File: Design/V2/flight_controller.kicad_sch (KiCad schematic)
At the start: 45 parts, among them J1 Conn_03x08_Odd_Even, J2 Conn_03x08_Odd_Even, U1 STM32H747BIT6

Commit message: power board
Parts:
- removed J1, J2: Conn_03x08_Odd_Even, symbol 3x8_Pin_Header:Conn_03x08_Odd_Even
- removed R10, R9: 4.7K, Resistor_SMD:R_0603_1608Metric_Pad0.98x0.95mm_HandSolder, symbol Device:R
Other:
- note removed: "I2C Pull-Up Resistors"

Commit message: editing bom
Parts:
- BARO1: LCSC Part # (none) -> C5124834
- C42, C43, C44, C47, C48, C49: LCSC Part # (none) -> C14663
- C45: LCSC Part # (none) -> C15849; Manufacturer_Part_Number CL10B105KO8NNNC -> CL10A105KB8NNNC
- C46: LCSC Part # (none) -> C15850; Manufacturer_Name KEMET -> Samsung Electro-Mechanics; Manufacturer_Part_Number C0805C106K8RACTU -> CL21A106KAYNNNE
- FLASH1: Height 0.8 -> (none); Mouser Part Number 454-W25N01GWZEIG -> (none); Mouser Price/Stock https://www.mouser.co.uk/ProductDetail/Winbond/W25N01GWZEIG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 -> (none)
- IMU1: LCSC Part # (none) -> C5368700
- LED3, LED7: value R -> Red; LCSC Part # (none) -> C2286; Manufacturer_Name Lite-On Inc. -> Hubei KENTO Elec; Manufacturer_Part_Number LTST-C191KRKT -> KT-0603R
- LED4: value Y -> Red; LCSC Part # (none) -> C2286; Manufacturer_Name Lite-On Inc. -> Hubei KENTO Elec; Manufacturer_Part_Number LTST-C191KSKT -> KT-0603R
- LED5, LED6: value B -> Red; LCSC Part # (none) -> C2286; Manufacturer_Name Lite-On Inc. -> Hubei KENTO Elec; Manufacturer_Part_Number LTST-C193TBKT-5A -> KT-0603R
- MAG1: LCSC Part # (none) -> C404329
- R13, R14: LCSC Part # (none) -> C25804; Manufacturer_Name TE Connectivity Passive Product -> UNI-ROYAL(Uniroyal Elec); Manufacturer_Part_Number CRGP0603F10K -> 0603WAF1002T5E
- R15, R16, R17, R18, R19: value 330 -> 39; LCSC Part # (none) -> C2907032; Manufacturer_Name TE Connectivity Passive Product -> FOJAN; Manufacturer_Part_Number CRGP0603F330R -> FRC0603F39R0TS
- U1: LCSC Part # (none) -> C730197

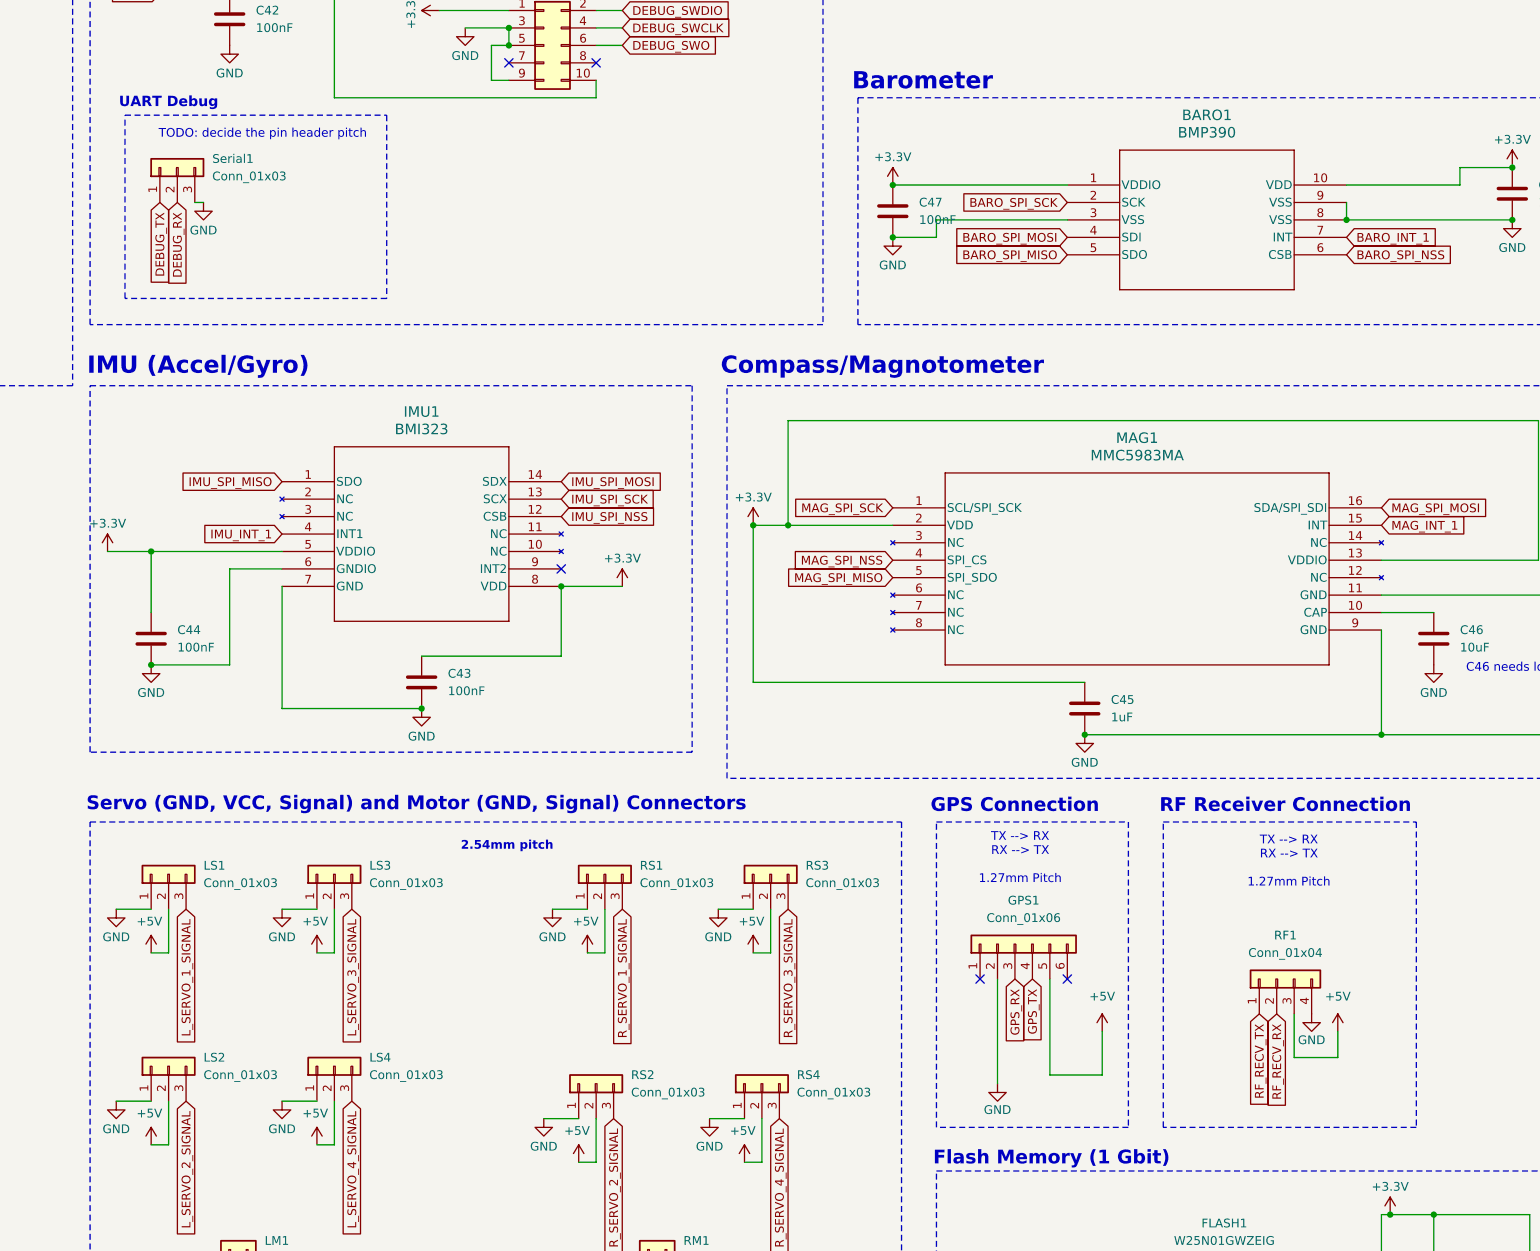
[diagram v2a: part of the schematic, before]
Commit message: added test pads for gps rf and debug
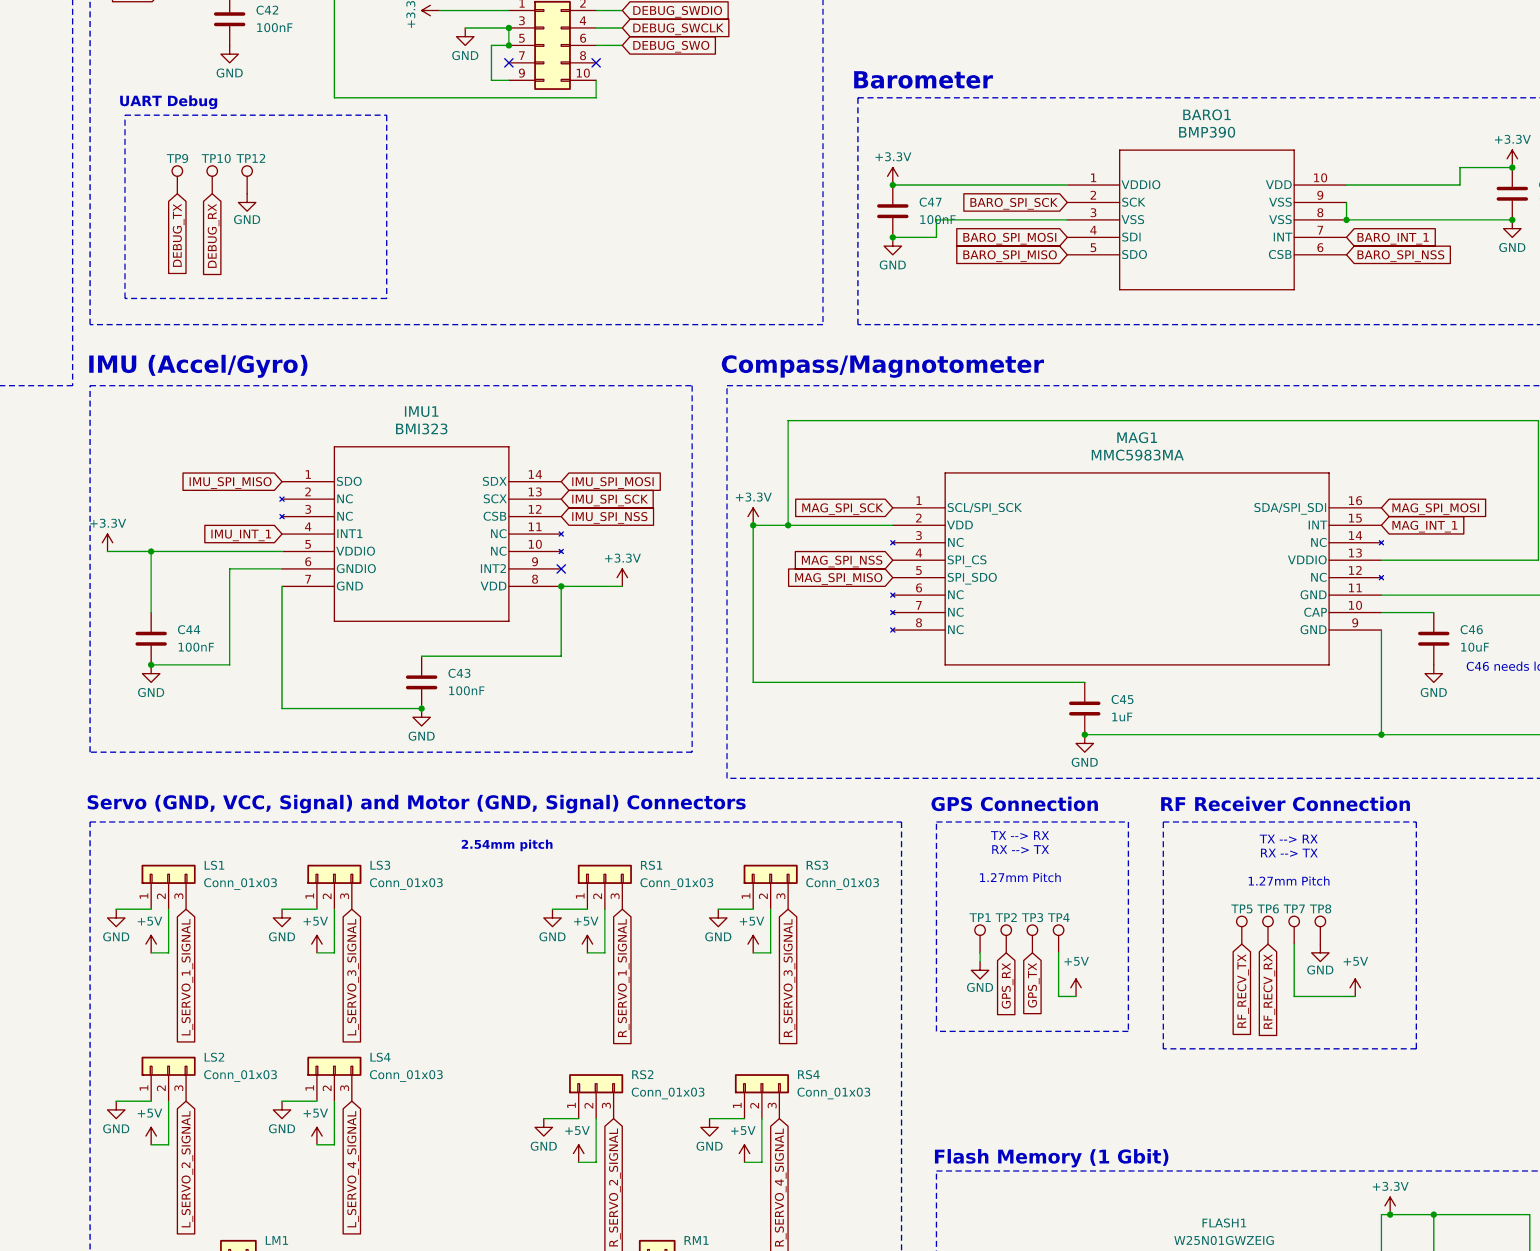
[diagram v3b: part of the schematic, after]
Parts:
- removed GPS1: Conn_01x06, Molex:CONN_532610001-SD_06Pin_1.25mm, symbol Connector_Generic:Conn_01x06
- removed RF1: Conn_01x04, Molex:CONN_532610471_SMD_4Pin_1.25mm, symbol Connector_Generic:Conn_01x04
- removed Serial1: Conn_01x03, Connector_PinHeader_2.54mm:PinHeader_1x03_P2.54mm_Vertical, symbol Connector_Generic:Conn_01x03
- added TP1, TP10, TP12, TP2, TP3, TP4, TP5, TP6, TP7, TP8, TP9: TestPoint, TestPoint:TestPoint_Pad_1.0x1.0mm, symbol Connector:TestPoint
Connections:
- net +5V: now also TP4.1, TP7.1
- net DEBUG_RX: now also TP10.1
- net DEBUG_TX: now also TP9.1
- net GND: now also TP1.1, TP12.1, TP8.1
- net GPS_RX: now also TP2.1
- net GPS_TX: now also TP3.1
- net RF_RECV_RX: now also TP6.1
- net RF_RECV_TX: now also TP5.1
- no-connect marks 113 -> 111
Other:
- note removed: "TODO: decide the pin header pitch"
